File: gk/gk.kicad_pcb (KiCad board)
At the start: 4 copper layers, 108 x 158.8 mm, 177 parts, among them J1 USB_C_Receptacle_USB2.0, J2 Conn_01x02, J3 Conn_02x27_Top_Bottom, J4 Micro_SD_Card_Det2, J5 AudioJack3_SwitchTR, J6 Conn_01x02, J7 Conn_01x02, J8 Conn_ARM_JTAG_SWD_10, SW1 SW_Push, SW2 SW_Push, U1 WE-TVS-82400102, U2 MCP73831-2-OT, U3 AP62300WU, U4 STM32H747BITx, U5 PT4110E89E, U6 IS42S16320F-7TLI-TR, U7 PCM1754DBQ, U8 PAM8008, U9 LSM6DSL, Y1 16MHz

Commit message: sdram routing
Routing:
- net VCC: track 0.00 -> 156.2 mm, vias 0 -> 2
- net GND: track 0.00 -> 106.5 mm, vias 0 -> 38
- net USB_D_N: track 0.00 -> 102.1 mm, vias 0 -> 3
- net USB_D_P: track 0.00 -> 102.0 mm, vias 0 -> 3
- net USB_VBUS: track 0.00 -> 70.9 mm, vias 0 -> 5
- net Net-(D1-K): track 0.00 -> 45.6 mm, vias 0 -> 4
- net FMC_D0: track 0.00 -> 37.8 mm, vias 0 -> 4
- net FMC_SDNWE: track 0.00 -> 36.3 mm, vias 0 -> 4
- net FMC_D1: track 0.00 -> 35.4 mm, vias 0 -> 3
- net FMC_SDNE0: track 0.00 -> 34.0 mm, vias 0 -> 4
- net VCORE: track 0.00 -> 32.7 mm
- net FMC_A3: track 0.00 -> 32.3 mm, vias 0 -> 3
- net FMC_SDNRAS: track 0.00 -> 32.3 mm, vias 0 -> 4
- net FMC_A10: track 0.00 -> 31.2 mm, vias 0 -> 4
- net FMC_A2: track 0.00 -> 31.1 mm, vias 0 -> 3
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
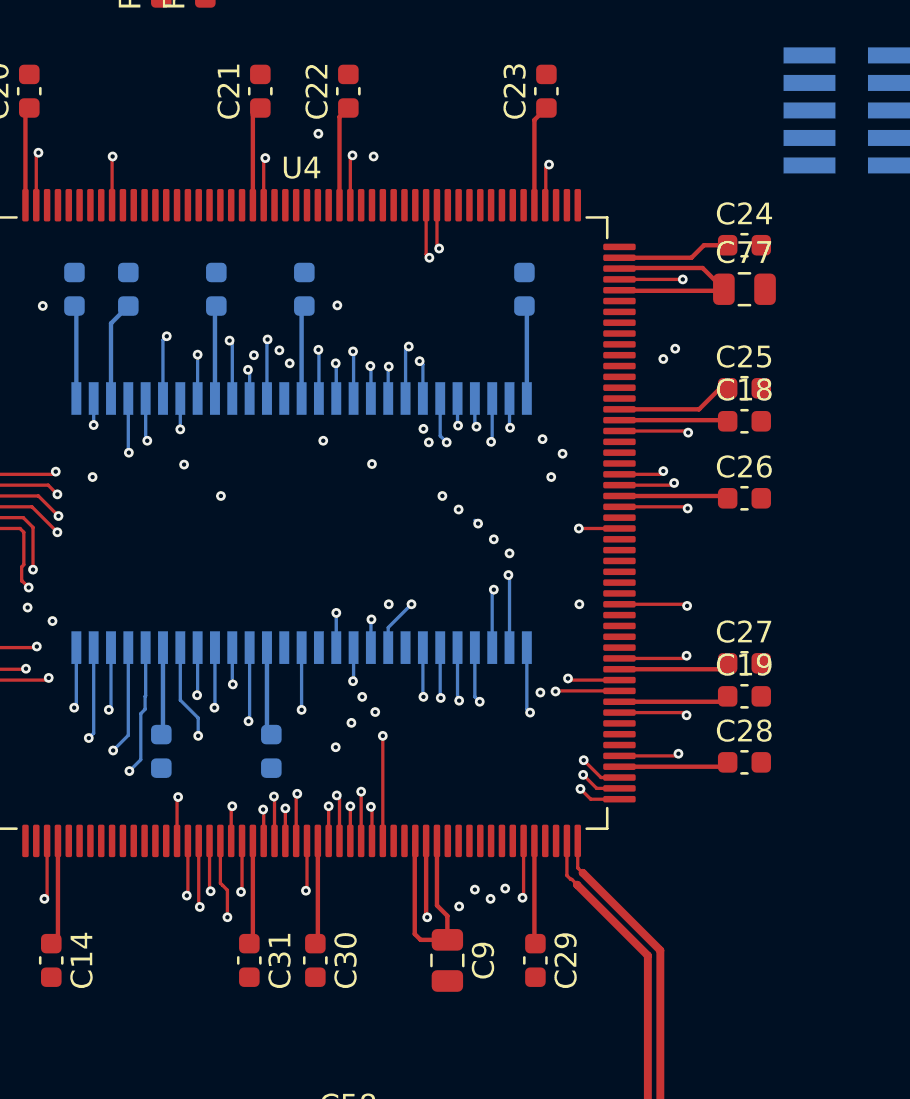
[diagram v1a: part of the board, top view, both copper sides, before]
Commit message: sdram post length matching
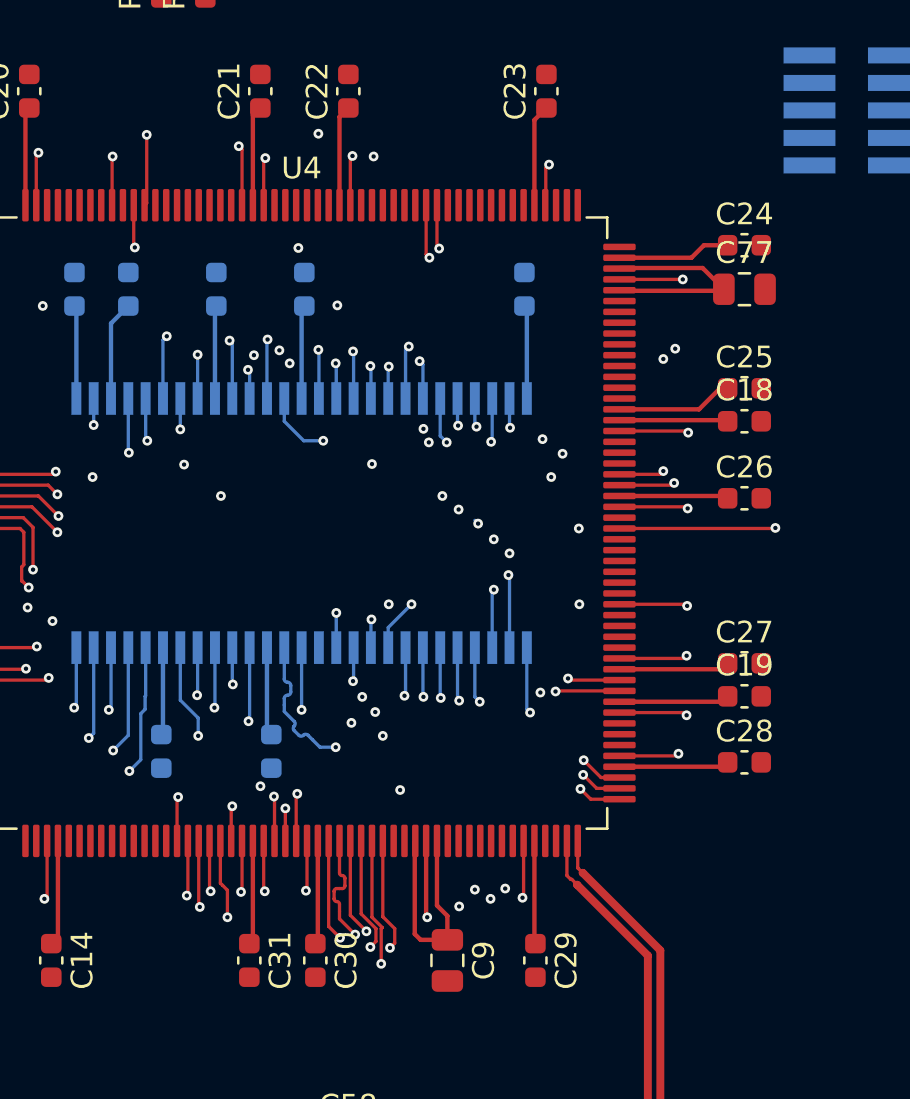
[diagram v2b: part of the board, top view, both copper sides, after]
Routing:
- net FMC_NBL1: track 1.60 -> 29.0 mm, vias 1 -> 3
- net FMC_A12: track 15.6 -> 37.5 mm, vias 3 -> 4
- net FMC_A11: track 1.46 -> 22.3 mm, vias 1 -> 4
- net FMC_D8: track 6.36 -> 22.9 mm
- net FMC_D7: track 18.6 -> 32.8 mm
- net FMC_SDNCAS: track 11.6 -> 24.4 mm, vias 2 -> 3
- net FMC_D11: track 16.8 -> 28.6 mm
- net FMC_NBL0: track 12.2 -> 23.5 mm, vias 2 -> 3
- net FMC_D10: track 14.7 -> 25.2 mm
- net FMC_D12: track 17.8 -> 28.2 mm, vias 2 -> 3
- net FMC_SDCLK: track 22.2 -> 31.5 mm
- net FMC_D9: track 13.7 -> 22.6 mm
- net FMC_A0: track 28.0 -> 34.3 mm
- net FMC_BA1: track 20.3 -> 26.5 mm
- net FMC_D6: track 25.6 -> 31.2 mm
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
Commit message: Update pcb
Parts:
- added C78: 100n, Capacitor_SMD:C_0603_1608Metric, F.Cu at (63.3, 102.1)
- added D5: D, Diode_SMD:D_SOD-128, B.Cu at (90.9, 162.8)
- added D6: D_TVS, Diode_SMD:D_SMA, B.Cu at (83.1, 163.6)
- added J10: Barrel_Jack_Switch, Connector_BarrelJack:BarrelJack_Horizontal, B.Cu at (84.5, 168.2)
- added J9: Conn_01x06, Connector_FFC-FPC:TE_0-1734839-6_1x06-1MP_P0.5mm_Horizontal, F.Cu at (65.9, 109.1)
- added R56: 10k, Resistor_SMD:R_0603_1608Metric, F.Cu at (64.6, 95.5)
- moved R8 38.6 mm to (79.8, 49.8)
- moved C75 20.2 mm to (52.5, 85.2)
- moved R52 20.2 mm to (52.5, 88.2)
- moved R53 20.2 mm to (52.5, 91.2)
- moved C76 20.2 mm to (56.5, 85.1)
- moved R54 20.2 mm to (56.5, 88.2)
- moved R55 20.2 mm to (56.5, 90.7)
- moved R9 8.33 mm to (50.3, 68.9)
- moved R23 4.44 mm to (90.2, 45.7)
- moved R24 3.87 mm to (90.2, 42.3), turned to -90 degrees
- moved R19 1.76 mm to (79.3, 38.2), turned to -90 degrees
- moved C58 1.08 mm to (101.3, 95.8), turned to 90 degrees
- turned C11 to 180 degrees
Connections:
- U4 pad 10: unconnected-(U4-PC13-Pad10) -> CTP_NRESET
- U4 pad 11: unconnected-(U4-PC14-Pad11) -> CTP_INT
- U4 pad 149: unconnected-(U4-PA11-Pad149) -> LED_BACKLIGHT_PWM
- U4 pad 166: unconnected-(U4-PA15-Pad166) -> SDMMC_DETECT
- U4 pad 45: unconnected-(U4-PA0-Pad45) -> SPKR_VOLUME
- U4 pad 57: SPKR_VOLUME -> unconnected-(U4-PA4-Pad57)
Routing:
- net GND: track 106.4 -> 397.6 mm, vias 38 -> 150
- net USB_VBUS: track 70.9 -> 276.3 mm, vias 5 -> 6
- net SPI1_MISO: track 0.00 -> 184.4 mm, vias 0 -> 1
- net BTN_MCU_MENU: track 0.00 -> 183.7 mm, vias 0 -> 7
- net SPI1_MOSI: track 0.00 -> 179.0 mm, vias 0 -> 1
- net SPI1_NSS: track 0.00 -> 178.8 mm, vias 0 -> 1
- net SPI1_SCK: track 0.00 -> 178.8 mm, vias 0 -> 1
- net WIFI_IRQ: track 0.00 -> 171.6 mm, vias 0 -> 6
- net VCC: track 156.2 -> 317.7 mm, vias 2 -> 62
- net Net-(D1-A): track 29.8 -> 183.4 mm, vias 0 -> 3
- net NRST: track 0.00 -> 151.5 mm, vias 0 -> 5
- net LED_BACKLIGHT_PWM: track 0.00 -> 148.5 mm, vias 0 -> 5
- net BTN_MCU_R: track 0.00 -> 144.0 mm, vias 0 -> 7
- net I2C4_SCL: track 0.00 -> 141.0 mm, vias 0 -> 5
- net I2C4_SDA: track 0.00 -> 136.5 mm, vias 0 -> 5
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- added copper zone on In1.Cu, net GND
- added copper zone on In4.Cu, net GND
- added copper zone on In2.Cu, net VCC
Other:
- copper layers 4 -> 6

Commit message: Update pcb
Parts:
- added C79: 100n, Capacitor_SMD:C_0603_1608Metric, B.Cu at (118.3, 168.5)
- added J11: Conn_01x02, Connector_JST:JST_XH_S2B-XH-A_1x02_P2.50mm_Horizontal, B.Cu at (49.4, 169.7)
- added R57: 10k, Resistor_SMD:R_0603_1608Metric, B.Cu at (50.2, 176.1)
- added SW3: RotaryEncoder_Switch, Rotary_Encoder:RotaryEncoder_Alps_EC11E-Switch_Vertical_H20mm, F.Cu at (58.8, 126.4)
- added U10: MAX17048, Package_DFN_QFN:TDFN-8-1EP_2x2mm_P0.5mm_EP0.8x1.2mm, B.Cu at (113.4, 173.9)
- moved C69 13.0 mm to (55.3, 141.5)
- moved R40 13.0 mm to (55.3, 144.6)
- moved R41 13.0 mm to (55.3, 143.1)
- moved D4 0.61 mm to (63.6, 120.0)
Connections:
- U4 pad 162: LSM6DSL_INT2 -> WIFI_IRQ
- U4 pad 2: WIFI_IRQ -> unconnected-(U4-PE3-Pad2)
- U4 pad 60: unconnected-(U4-PA7-Pad60) -> NTC_MCU
- U9 pad 9: LSM6DSL_INT2 -> unconnected-(U9-INT2-Pad9)
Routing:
- net NTC_MCU: track 0.00 -> 122.5 mm, vias 0 -> 1
- net LSM6DSL_INT2: track 109.2 -> 0.00 mm, vias 6 -> 0
- net I2C4_SCL: track 141.0 -> 248.2 mm, vias 5 -> 7
- net I2C4_SDA: track 136.5 -> 242.9 mm, vias 5 -> 8
- net Net-(R38-Pad2): track 11.3 -> 67.1 mm
- net Net-(R40-Pad2): track 11.2 -> 56.0 mm
- net Net-(R36-Pad2): track 11.8 -> 33.3 mm
- net GND: track 397.6 -> 412.5 mm, vias 150 -> 156
- net Net-(D1-A): track 183.4 -> 193.5 mm
- net VCC: track 317.7 -> 322.9 mm, vias 62 -> 63
- net BTN_MCU_L: track 111.1 -> 106.6 mm
- net Net-(D3-K): track 19.0 -> 22.7 mm
- net USB_VBUS: track 276.3 -> 278.1 mm
- net Net-(U4-VLXSMPS): track 18.1 -> 16.8 mm
- net Net-(D4-K): track 23.8 -> 23.2 mm
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
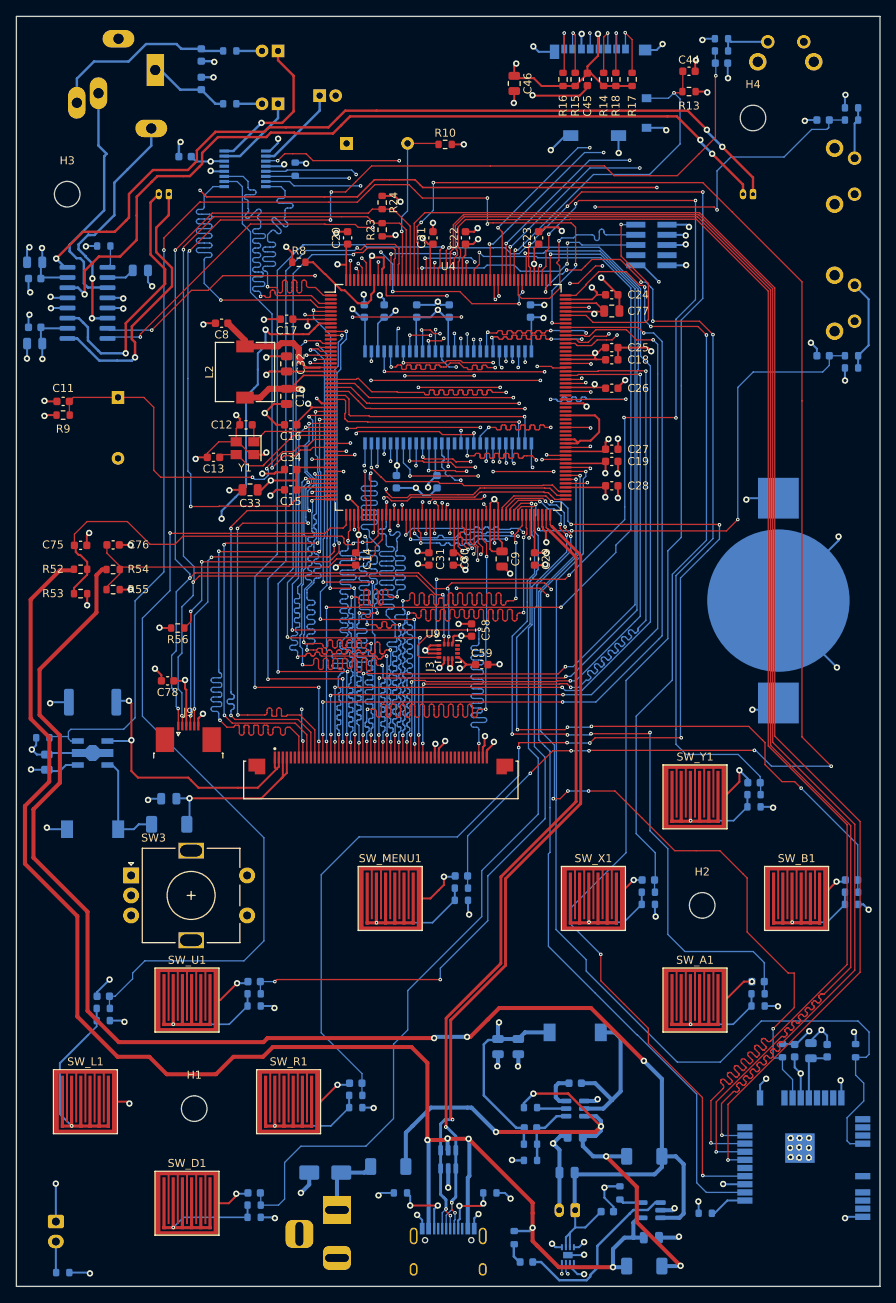
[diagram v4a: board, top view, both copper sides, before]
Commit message: Add mount pin for abxy/udlr buttons Fix button spacing Add leds for menu button
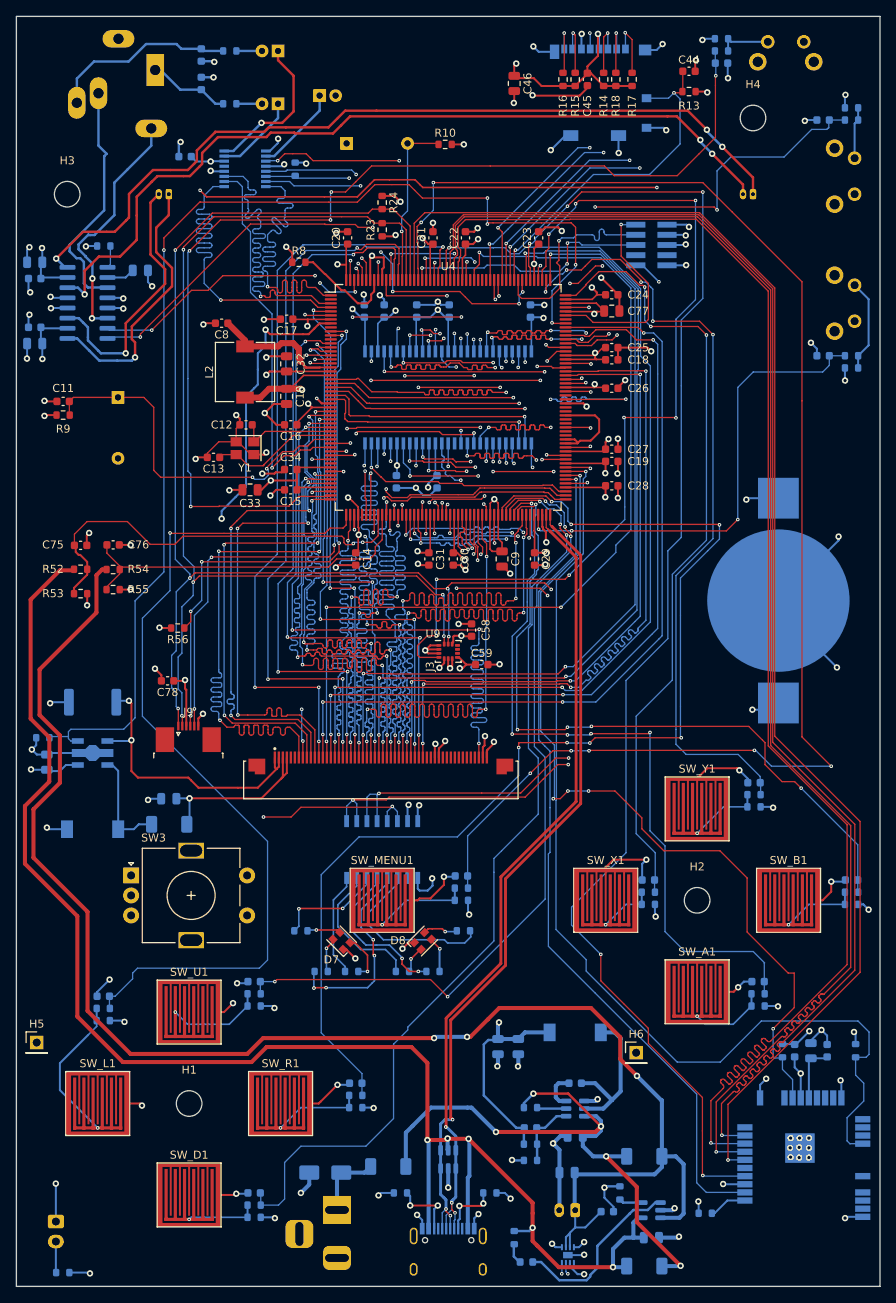
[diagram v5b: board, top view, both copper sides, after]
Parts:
- added D7: LED_ARGB, LED_SMD:LED_ASMB-KTF0-0A306, F.Cu at (85.1, 134.6)
- added D8: LED_ARGB, LED_SMD:LED_ASMB-KTF0-0A306, F.Cu at (95.2, 134.6)
- added H5: Conn_01x01, Connector_PinHeader_2.54mm:PinHeader_1x01_P2.54mm_Vertical, F.Cu at (47.0, 147.3)
- added H6: Conn_01x01, Connector_PinHeader_2.54mm:PinHeader_1x01_P2.54mm_Vertical, F.Cu at (121.9, 148.6)
- added R58: 130R, Resistor_SMD:R_0603_1608Metric, B.Cu at (92.7, 138.4)
- added R59: 35R, Resistor_SMD:R_0603_1608Metric, B.Cu at (96.5, 138.4)
- added R60: 45R, Resistor_SMD:R_0603_1608Metric, B.Cu at (100.3, 133.3)
- added R61: 130R, Resistor_SMD:R_0603_1608Metric, B.Cu at (86.4, 138.4)
- added R62: 35R, Resistor_SMD:R_0603_1608Metric, B.Cu at (80.0, 133.3)
- added R63: 45R, Resistor_SMD:R_0603_1608Metric, B.Cu at (82.5, 138.4)
- added U11: ULN2003A, Package_SO:SOIC-16W_5.3x10.2mm_P1.27mm, B.Cu at (90.2, 123.2)
- moved SW_L1 1.55 mm to (54.6, 154.9)
- moved SW_X1 1.55 mm to (118.1, 129.5)
- moved SW_U1 1.53 mm to (66.0, 143.5)
- moved SW_Y1 1.53 mm to (129.5, 118.1)
- moved SW_D1 1.07 mm to (66.0, 166.4)
- moved SW_A1 1.07 mm to (129.5, 141.0)
- moved SW_B1 1.03 mm to (141.0, 129.5)
- moved SW_MENU1 1.03 mm to (90.2, 129.5)
- moved SW_R1 1.03 mm to (77.5, 154.9)
- moved H2 0.90 mm to (129.5, 129.5)
- moved H1 0.90 mm to (66.0, 154.9)
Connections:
- U4 pad 142: unconnected-(U4-PC6-Pad142) -> BTNLED_R
- U4 pad 143: unconnected-(U4-PC7-Pad143) -> BTNLED_G
- U4 pad 206: unconnected-(U4-PI7-Pad206) -> BTNLED_B
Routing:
- net BTNLED_R: track 0.00 -> 104.2 mm, vias 0 -> 3
- net BTNLED_G: track 0.00 -> 102.5 mm, vias 0 -> 3
- net BTNLED_B: track 0.00 -> 97.5 mm, vias 0 -> 4
- net Net-(U11-O5): track 0.00 -> 25.0 mm, vias 0 -> 4
- net Net-(U11-O6): track 0.00 -> 22.1 mm
- net Net-(U11-O4): track 0.00 -> 19.7 mm, vias 0 -> 2
- net Net-(U11-O2): track 0.00 -> 17.5 mm
- net Net-(U11-O3): track 0.00 -> 13.6 mm, vias 0 -> 2
- net Net-(U11-O1): track 0.00 -> 13.0 mm
- net GND: track 412.5 -> 424.1 mm, vias 156 -> 159
- net Net-(R38-Pad2): track 67.1 -> 57.0 mm
- net VCC: track 322.9 -> 331.2 mm, vias 63 -> 66
- net Net-(D7-RK): track 0.00 -> 6.03 mm, vias 0 -> 1
- net Net-(D8-GK): track 0.00 -> 4.48 mm, vias 0 -> 1
- net Net-(D7-BK): track 0.00 -> 4.43 mm, vias 0 -> 1
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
